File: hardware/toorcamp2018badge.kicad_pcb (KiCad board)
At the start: 2 copper layers, 68.5 x 68.5 mm, 36 parts, among them P1 CONN_1, P10 CONN_1, P11 CONN_1, P12 CONN_1, P13 CONN_1, P14 CONN_1, P15 CONN_1, P16 CONN_1, P17 CONN_1, P18 CONN_1, P19 JTAG, P2 CONN_1, P20 CONN_2X2, P3 CONN_1, P4 CONN_1, P5 CONN_1, P6 CONN_1, P7 CONN_1, P8 CONN_1, P9 CONN_1, U1 MSP430G2211

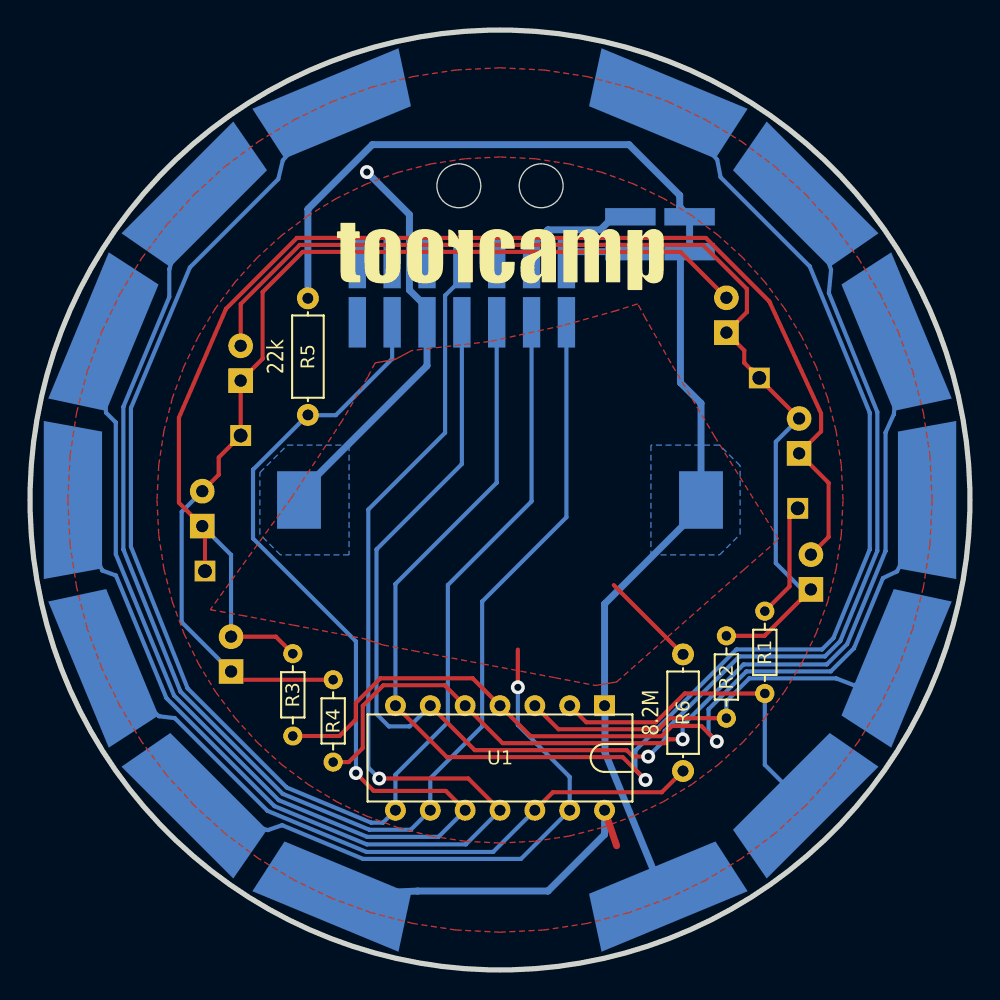
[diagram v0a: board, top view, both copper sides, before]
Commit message: removed ToorCamp logos and event information
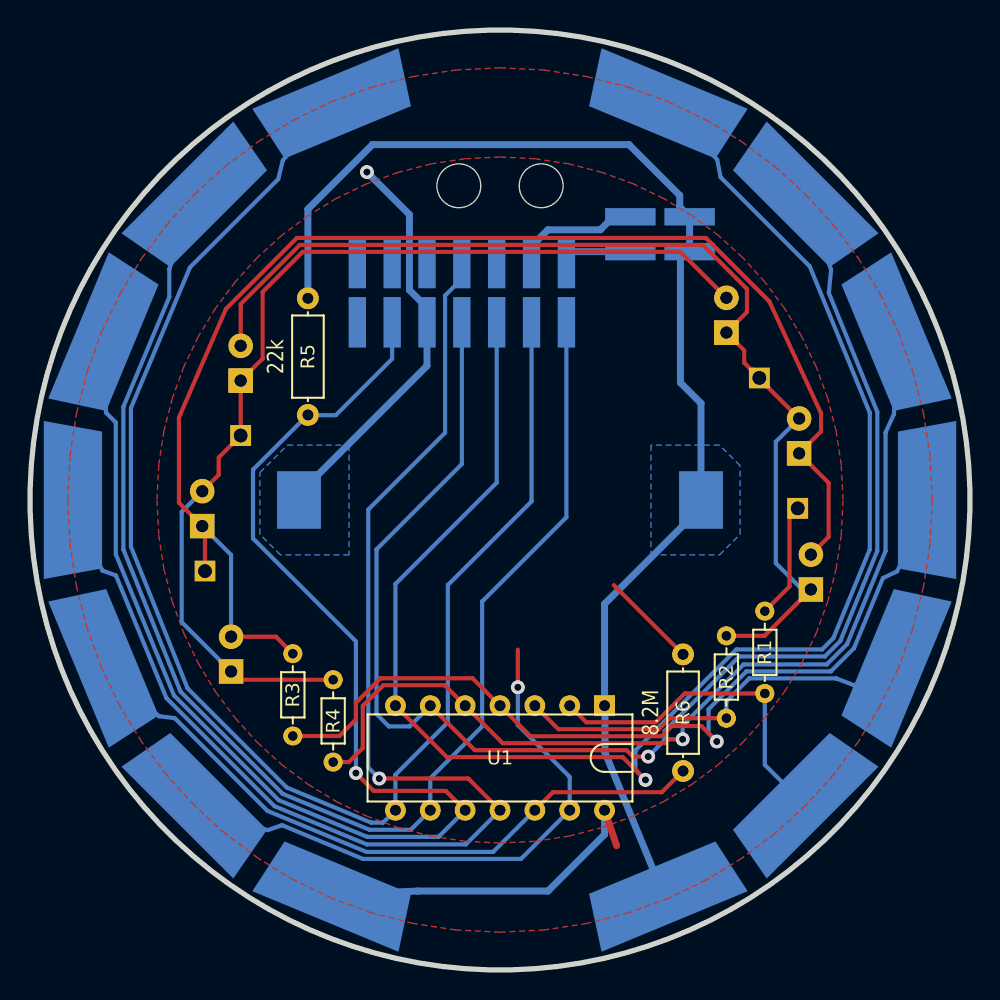
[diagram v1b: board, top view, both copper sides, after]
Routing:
- removed copper zone on F.Cu, net /P2.6
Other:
- board text added: "variant of ToorCamp 2018 Badge"
- board text removed: "2018"
- board text removed: "badge sponsors: Great Scott Gadgets and OSH Park"

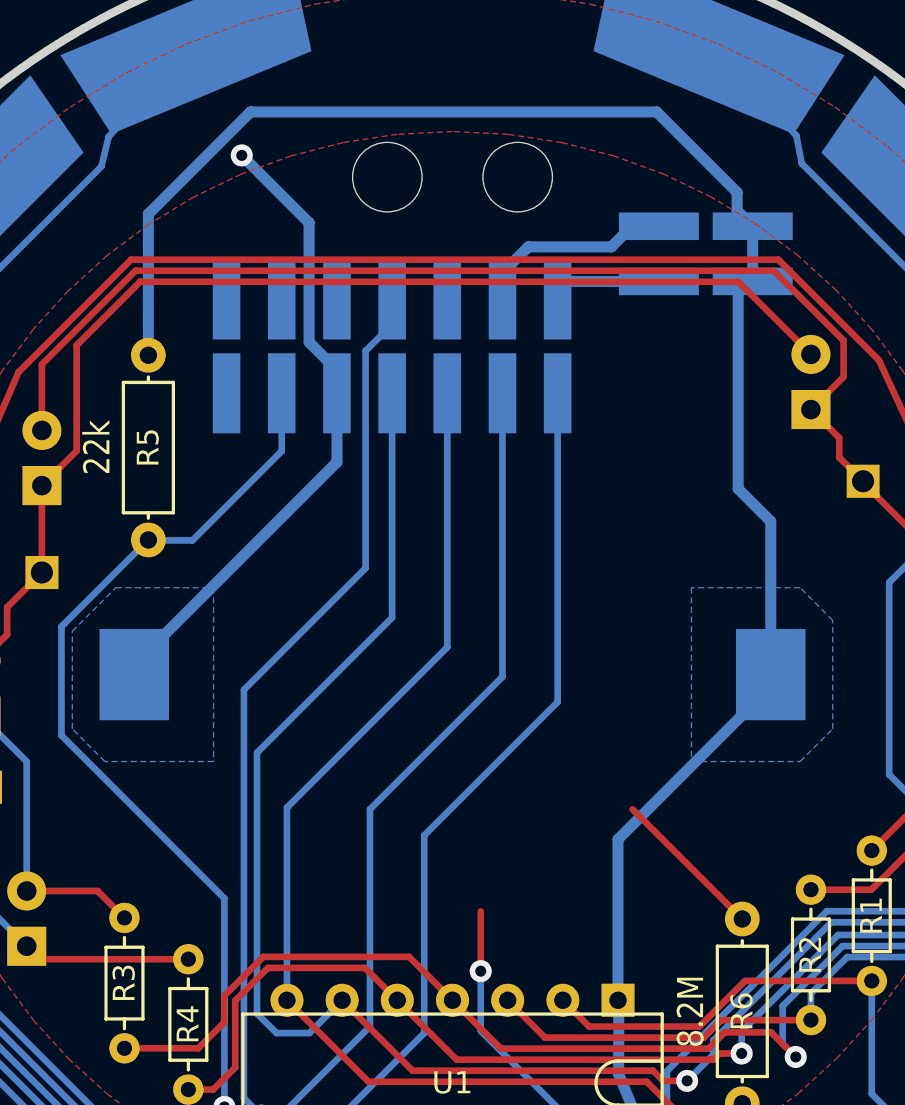
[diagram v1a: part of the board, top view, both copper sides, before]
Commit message: added Great Scott Gadgets gear logo
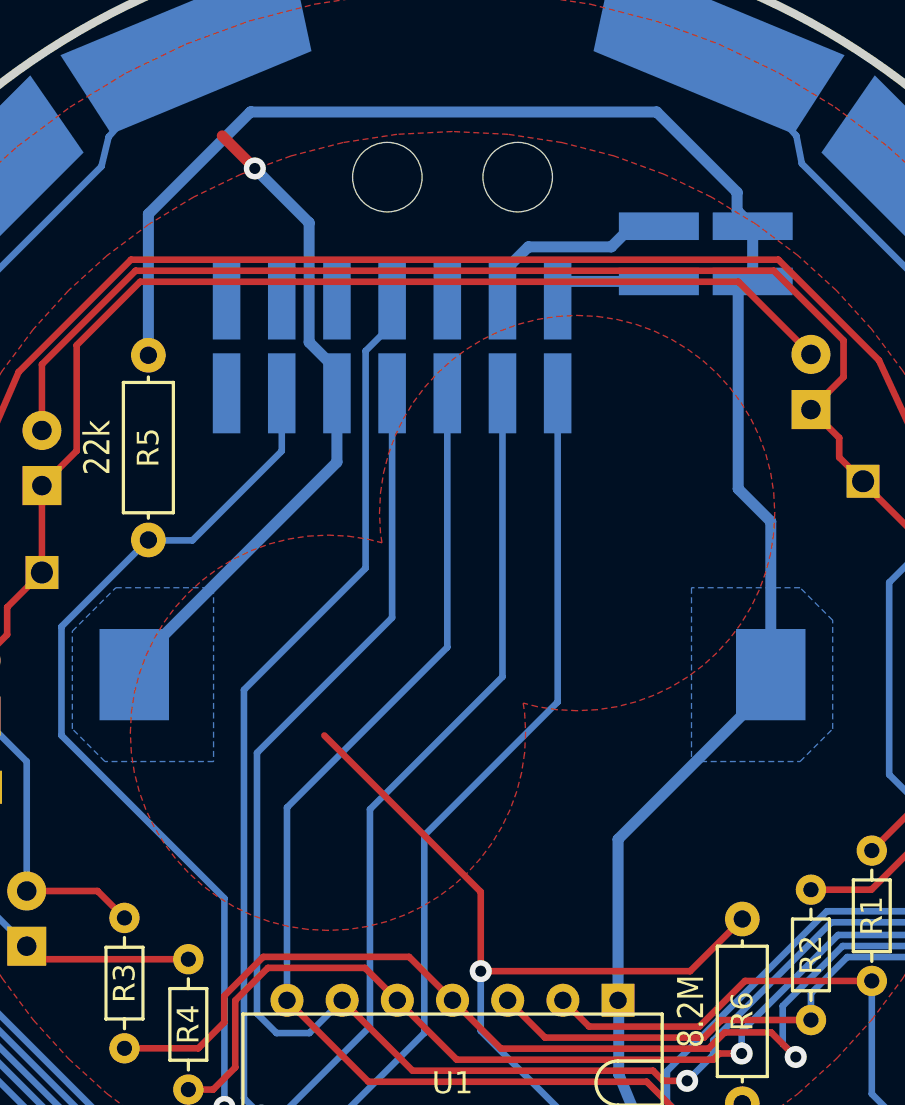
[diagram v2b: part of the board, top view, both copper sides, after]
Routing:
- net /P2.6: track 50.1 -> 67.1 mm
- net GND: track 55.9 -> 57.2 mm
- added copper zone on F.Cu, net /P2.6
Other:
- board text added: "20180509"
- board text added: "Great Scott Gadgets logo variant of ToorCamp 2018 Badge"
- board text removed: "20180508"
- board text removed: "variant of ToorCamp 2018 Badge"

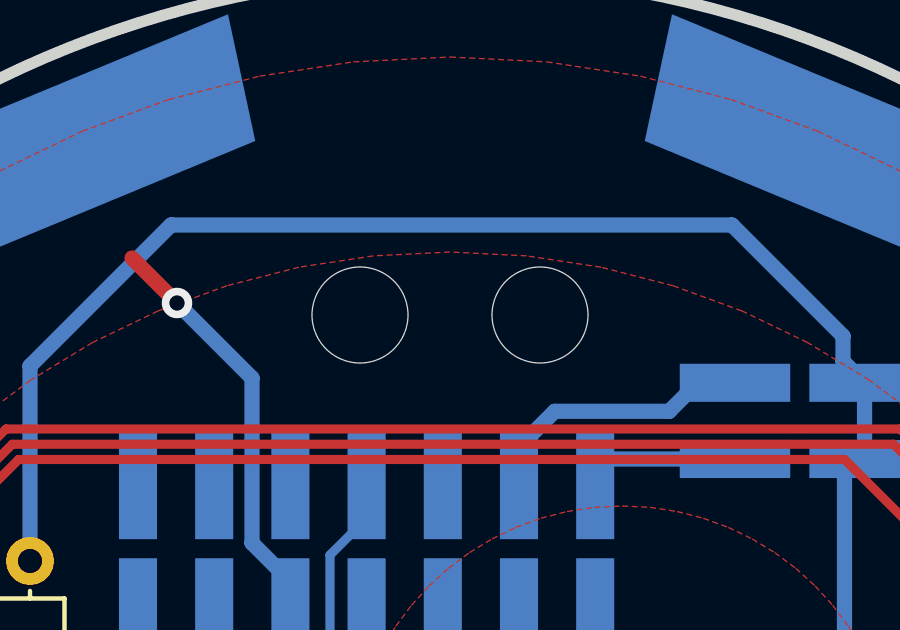
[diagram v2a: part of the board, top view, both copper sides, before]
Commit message: removed lanyard holes
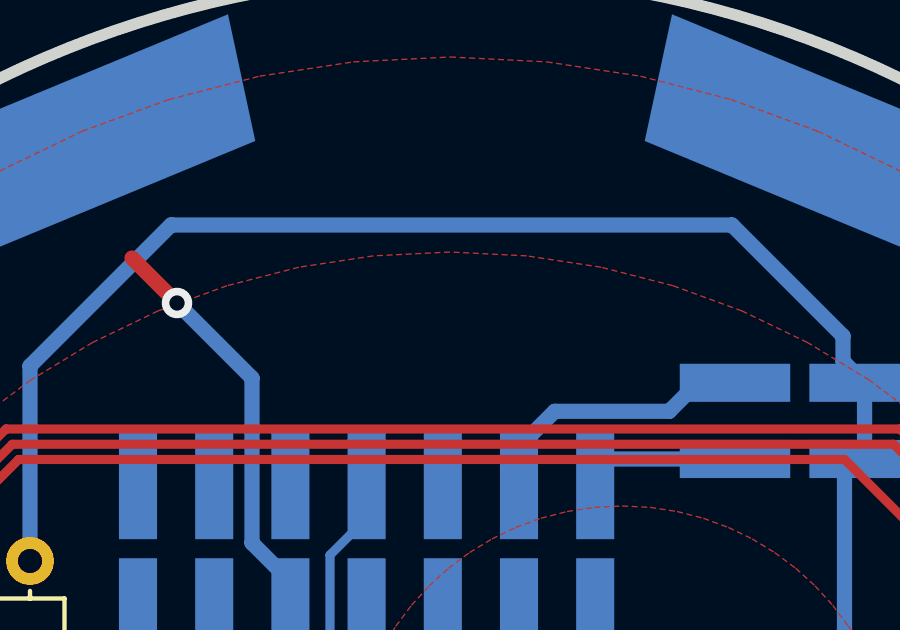
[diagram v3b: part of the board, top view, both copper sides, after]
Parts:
- removed REF** (x2): MountingHole_3.2mm_M3, Mounting_Holes:MountingHole_3.2mm_M3
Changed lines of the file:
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@@
     (links 65)
     (no_connects 0)
-    (area 115.559499 65.559499 184.440501 134.440501)
+    (area 108.809499 61.809499 191.190501 141.190501)
     (thickness 1.6002)
     (drawings 48)
     (tracks 275)
     (zones 0)
-    (modules 36)
+    (modules 34)
     (nets 21)
   )
@@
   )
   (setup
-    (last_trace_width 0.508)
+    (last_trace_width 0.3048)
     (user_trace_width 0.2032)
     (user_trace_width 0.508)
@@
     (add_net VCC)
   )
-  (module Mounting_Holes:MountingHole_3.2mm_M3 (layer Front)
-    (at 147.2 77)
-    (descr "Mounting Hole 3.2mm, no annular, M3")
-    (tags "mounting hole 3.2mm no annular m3")
-    (attr virtual)
-    (fp_text reference REF** (at 0 -4.2) (layer F.SilkS) hide
-      (effects (font (size 1 1) (thickness 0.15)))
-    )
-    (fp_text value MountingHole_3.2mm_M3 (at 0 4.2) (layer F.Fab) hide
-      (effects (font (size 1 1) (thickness 0.15)))
-    )
-    (fp_text user %R (at 0.3 0) (layer F.Fab)
-      (effects (font (size 1 1) (thickness 0.15)))
-    )
-    (fp_circle (center 0 0) (end 3.2 0) (layer Cmts.User) (width 0.15))
-    (fp_circle (center 0 0) (end 3.45 0) (layer F.CrtYd) (width 0.05))
-    (pad "" np_thru_hole circle (at -0.2 0.1) (size 3.2 3.2) (drill 3.2) (layers *.Cu *.Mask))
-  )
-  (module Mounting_Holes:MountingHole_3.2mm_M3 (layer Front)
-    (at 152.8 77)
-    (descr "Mounting Hole 3.2mm, no annular, M3")
-    (tags "mounting hole 3.2mm no annular m3")
-    (attr virtual)
-    (fp_text reference REF** (at 0 -4.2) (layer F.SilkS) hide
-      (effects (font (size 1 1) (thickness 0.15)))
-    )
-    (fp_text value MountingHole_3.2mm_M3 (at 0 4.2) (layer F.Fab) hide
-      (effects (font (size 1 1) (thickness 0.15)))
-    )
-    (fp_text user %R (at 0.3 0) (layer F.Fab)
-      (effects (font (size 1 1) (thickness 0.15)))
-    )
-    (fp_circle (center 0 0) (end 3.2 0) (layer Cmts.User) (width 0.15))
-    (fp_circle (center 0 0) (end 3.45 0) (layer F.CrtYd) (width 0.05))
-    (pad "" np_thru_hole circle (at 0.2 0.1) (size 3.2 3.2) (drill 3.2) (layers *.Cu *.Mask))
-  )
   (module gsg-modules:BU2032SM-BT (layer Back)
